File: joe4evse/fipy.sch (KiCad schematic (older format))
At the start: 2 parts

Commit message: joe/sch: Schematic should be done
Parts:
- added C4, C9: 100n, Capacitor_SMD:C_0603_1608Metric, symbol Device:C_Small
- added D3, D4: Green, LED_SMD:LED_0603_1608Metric, symbol Device:LED
- added R3, R4: 1k, Resistor_SMD:R_0603_1608Metric, symbol Device:R_Small
- added U4: MCP23S08-SO, Package_SO:SOIC-18W_7.5x11.6mm_P1.27mm, symbol ma4evse:MCP23S08-SO
- gave numbers to parts that had none: 2
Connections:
- net NFC_NRSTOUT is gone; now on net NFC_IRQ: U3.15 (P13)
- net +3V3: now also C4.2, C9.2, D3.2 (A), U4.18 (VCC)
- net +5V: now also D4.2 (A)
- net GND: now also C4.1, C9.1, R3.2, R4.2, U4.4 (A1), U4.5 (A0), U4.9 (GND)
- net MOD_EN: now also U4.12 (IO2); no longer U3.24 (P22)
- net NFC_IRQ: no longer U3.18 (P16)
- net FIPY_RX renamed RXD
- net FIPY_TX renamed TXD
- net FTDI_RX renamed LED_~CS
- net FTDI_TX renamed NFC_~CS
- net GPIO_P12: no longer names the net of U3.14 (ANT/P12)
- net GPIO_P2 renamed DEV_~RST
- net DEV_~RST: now also U4.6 (~RST)
- net GPIO_P21 renamed PP_IN
- net NFC_CLK renamed SCLK
- net SCLK: now also U4.1 (SCK)
- net NFC_MISO renamed MISO
- net MISO: now also U4.3 (SOUT)
- net NFC_MOSI renamed MOSI
- net MOSI: now also U4.2 (SIN)
- net NFC_NRST renamed IO_~CS
- net IO_~CS: now also U4.7 (~CS)
- net NFC_SS renamed TEMP
- net RELAY renamed PILOT_IN
- new net: D3.1 (K), R3.1
- new net: D4.1 (K), R4.1
- new net AC_TEST0: U4.14 (IO4)
- new net AC_TEST1: U4.15 (IO5)
- new net IO_IRQ: U3.18 (P16), U4.8 (INT)
- new net PILOT_OUT: U3.24 (P22)
- new net RCMB_AC_30mA: U4.17 (IO7)
- new net RCMB_DC_6mA: U4.16 (IO6)
- new net RELAY_AC: U4.11 (IO1)
- new net RELAY_JACK: U4.10 (IO0)
- new net TOUCH: U4.13 (IO3)
- no-connect marks 8 -> 9
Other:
- note added: "AC power verification signals"
- note added: "Charge port signals"
- note added: "Global SPI bus"
- note added: "Misc device control signals"
- note added: "Misc devices data signals"
- note added: "Power relays signals"
- note added: "Power status LEDs"
- note added: "Programming/ModBUS combined UART"
- note removed: "DHT11"
- note removed: "pin_out = \nP10\nP11\nP12\nP8\nP9"
- note removed: "uartm == UART0 = EV Controller\nSPI_PINS = RFID @1M == P10 P11 P12\nModbus = SmartMeter\n"
- moved on the sheet: J8, U3

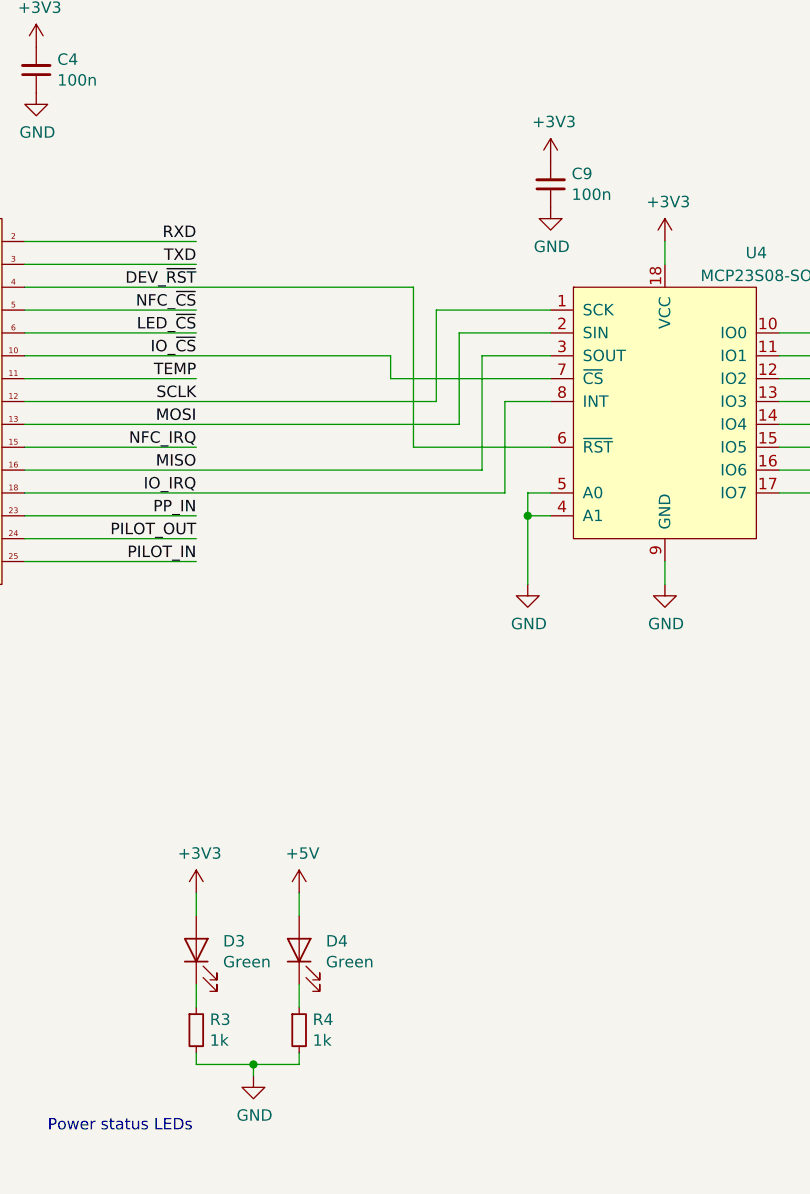
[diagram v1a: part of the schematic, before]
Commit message: joe/sch: Assign footprints to components
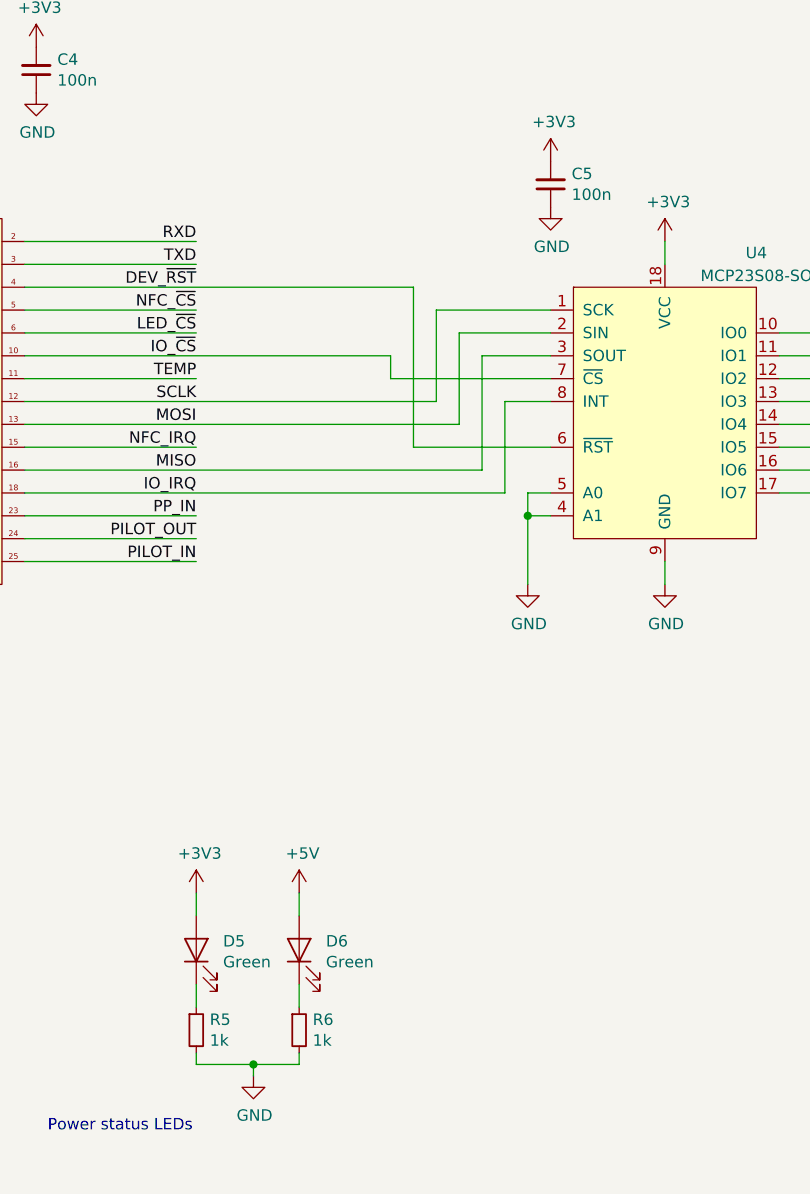
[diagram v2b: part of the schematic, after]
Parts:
- renumbered C9 to C5, D3 to D5, D4 to D6, R3 to R5, R4 to R6
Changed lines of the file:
@@
 	2800 2150 2900 2150
 $Comp
-L power:GND #PWR016
+L power:GND #PWR033
 U 1 1 5DD69575
 P 2900 2250
-F 0 "#PWR016" H 2900 2000 50  0001 C CNN
+F 0 "#PWR033" H 2900 2000 50  0001 C CNN
 F 1 "GND" H 2905 2077 50  0000 C CNN
 F 2 "" H 2900 2250 50  0001 C CNN
@@
 	4950 3550 4950 3650
 $Comp
-L power:GND #PWR019
+L power:GND #PWR036
 U 1 1 5DD69582
 P 4950 3650
-F 0 "#PWR019" H 4950 3400 50  0001 C CNN
+F 0 "#PWR036" H 4950 3400 50  0001 C CNN
 F 1 "GND" H 4955 3477 50  0000 C CNN
 F 2 "" H 4950 3650 50  0001 C CNN
@@
 	4850 1650 4850 1750
 $Comp
-L power:+3V3 #PWR014
+L power:+3V3 #PWR030
 U 1 1 5DD6958A
 P 5050 1650
-F 0 "#PWR014" H 5050 1500 50  0001 C CNN
+F 0 "#PWR030" H 5050 1500 50  0001 C CNN
 F 1 "+3V3" H 5065 1823 50  0000 C CNN
 F 2 "" H 5050 1650 50  0001 C CNN
@@
 $EndComp
 $Comp
-L power:+5V #PWR013
+L power:+5V #PWR029
 U 1 1 5DD69590
 P 4850 1650
-F 0 "#PWR013" H 4850 1500 50  0001 C CNN
+F 0 "#PWR029" H 4850 1500 50  0001 C CNN
 F 1 "+5V" H 4865 1823 50  0000 C CNN
 F 2 "" H 4850 1650 50  0001 C CNN
@@
 	5700 2450 7300 2450
 $Comp
-L power:GND #PWR017
+L power:GND #PWR034
 U 1 1 5E1CCCF4
 P 7900 3450
-F 0 "#PWR017" H 7900 3200 50  0001 C CNN
+F 0 "#PWR034" H 7900 3200 50  0001 C CNN
 F 1 "GND" H 7905 3277 50  0000 C CNN
 F 2 "" H 7900 3450 50  0001 C CNN
@@
 $EndComp
 $Comp
-L power:GND #PWR018
+L power:GND #PWR035
 U 1 1 5E1CD7DB
 P 8500 3450
-F 0 "#PWR018" H 8500 3200 50  0001 C CNN
+F 0 "#PWR035" H 8500 3200 50  0001 C CNN
 F 1 "GND" H 8505 3277 50  0000 C CNN
 F 2 "" H 8500 3450 50  0001 C CNN
@@
 $EndComp
 $Comp
-L power:+3V3 #PWR015
+L power:+3V3 #PWR032
 U 1 1 5E1CDD5F
 P 8500 1950
-F 0 "#PWR015" H 8500 1800 50  0001 C CNN
+F 0 "#PWR032" H 8500 1800 50  0001 C CNN
 F 1 "+3V3" H 8515 2123 50  0000 C CNN
 F 2 "" H 8500 1950 50  0001 C CNN
@@
 P 6450 5050
 AR Path="/5E261C05" Ref="D?"  Part="1"
-AR Path="/5DD371FF/5E261C05" Ref="D3"  Part="1"
-F 0 "D3" V 6489 4933 50  0000 R CNN
+AR Path="/5DD371FF/5E261C05" Ref="D5"  Part="1"
+F 0 "D5" V 6489 4933 50  0000 R CNN
 F 1 "Green" V 6398 4933 50  0000 R CNN
 F 2 "LED_SMD:LED_0603_1608Metric" H 6450 5050 50  0001 C CNN
@@
 P 6900 5050
 AR Path="/5E261C0B" Ref="D?"  Part="1"
-AR Path="/5DD371FF/5E261C0B" Ref="D4"  Part="1"
-F 0 "D4" V 6939 4933 50  0000 R CNN
+AR Path="/5DD371FF/5E261C0B" Ref="D6"  Part="1"
+F 0 "D6" V 6939 4933 50  0000 R CNN
 F 1 "Green" V 6848 4933 50  0000 R CNN
 F 2 "LED_SMD:LED_0603_1608Metric" H 6900 5050 50  0001 C CNN
@@
 P 6450 4800
 AR Path="/5E261C11" Ref="#PWR?"  Part="1"
-AR Path="/5DD371FF/5E261C11" Ref="#PWR020"  Part="1"
-F 0 "#PWR020" H 6450 4650 50  0001 C CNN
+AR Path="/5DD371FF/5E261C11" Ref="#PWR037"  Part="1"
+F 0 "#PWR037" H 6450 4650 50  0001 C CNN
 F 1 "+3V3" H 6465 4973 50  0000 C CNN
 F 2 "" H 6450 4800 50  0001 C CNN
@@
 P 6900 4800
 AR Path="/5E261C17" Ref="#PWR?"  Part="1"
-AR Path="/5DD371FF/5E261C17" Ref="#PWR021"  Part="1"
-F 0 "#PWR021" H 6900 4650 50  0001 C CNN
+AR Path="/5DD371FF/5E261C17" Ref="#PWR038"  Part="1"
+F 0 "#PWR038" H 6900 4650 50  0001 C CNN
 F 1 "+5V" H 6915 4973 50  0000 C CNN
 F 2 "" H 6900 4800 50  0001 C CNN
@@
 P 6450 5400
 AR Path="/5E261C1D" Ref="R?"  Part="1"
-AR Path="/5DD371FF/5E261C1D" Ref="R3"  Part="1"
-F 0 "R3" H 6509 5446 50  0000 L CNN
+AR Path="/5DD371FF/5E261C1D" Ref="R5"  Part="1"
+F 0 "R5" H 6509 5446 50  0000 L CNN
 F 1 "1k" H 6509 5355 50  0000 L CNN
 F 2 "Resistor_SMD:R_0603_1608Metric" H 6450 5400 50  0001 C CNN
@@
 P 6900 5400
 AR Path="/5E261C23" Ref="R?"  Part="1"
-AR Path="/5DD371FF/5E261C23" Ref="R4"  Part="1"
-F 0 "R4" H 6959 5446 50  0000 L CNN
+AR Path="/5DD371FF/5E261C23" Ref="R6"  Part="1"
+F 0 "R6" H 6959 5446 50  0000 L CNN
 F 1 "1k" H 6959 5355 50  0000 L CNN
 F 2 "Resistor_SMD:R_0603_1608Metric" H 6900 5400 50  0001 C CNN
@@
 P 6700 5600
 AR Path="/5E261C29" Ref="#PWR?"  Part="1"
-AR Path="/5DD371FF/5E261C29" Ref="#PWR022"  Part="1"
-F 0 "#PWR022" H 6700 5350 50  0001 C CNN
+AR Path="/5DD371FF/5E261C29" Ref="#PWR039"  Part="1"
+F 0 "#PWR039" H 6700 5350 50  0001 C CNN
 F 1 "GND" H 6705 5427 50  0000 C CNN
 F 2 "" H 6700 5600 50  0001 C CNN
@@
 P 5750 1100
 AR Path="/5E265A91" Ref="#PWR?"  Part="1"
-AR Path="/5DD371FF/5E265A91" Ref="#PWR011"  Part="1"
-F 0 "#PWR011" H 5750 950 50  0001 C CNN
+AR Path="/5DD371FF/5E265A91" Ref="#PWR026"  Part="1"
+F 0 "#PWR026" H 5750 950 50  0001 C CNN
 F 1 "+3V3" H 5765 1273 50  0000 C CNN
 F 2 "" H 5750 1100 50  0001 C CNN
@@
 P 5750 1300
 AR Path="/5E265A97" Ref="#PWR?"  Part="1"
-AR Path="/5DD371FF/5E265A97" Ref="#PWR012"  Part="1"
-F 0 "#PWR012" H 5750 1050 50  0001 C CNN
+AR Path="/5DD371FF/5E265A97" Ref="#PWR027"  Part="1"
+F 0 "#PWR027" H 5750 1050 50  0001 C CNN
 F 1 "GND" H 5755 1127 50  0000 C CNN
 F 2 "" H 5750 1300 50  0001 C CNN
@@
 P 8000 1700
 AR Path="/5E218F5F" Ref="C?"  Part="1"
-AR Path="/5DD371FF/5E218F5F" Ref="C9"  Part="1"
-F 0 "C9" H 7908 1654 50  0000 R CNN
+AR Path="/5DD371FF/5E218F5F" Ref="C5"  Part="1"
+F 0 "C5" H 7908 1654 50  0000 R CNN
 F 1 "100n" H 7908 1745 50  0000 R CNN
 F 2 "Capacitor_SMD:C_0603_1608Metric" H 8000 1700 50  0001 C CNN
@@
 P 8000 1600
 AR Path="/5E218F65" Ref="#PWR?"  Part="1"
-AR Path="/5DD371FF/5E218F65" Ref="#PWR0124"  Part="1"
-F 0 "#PWR0124" H 8000 1450 50  0001 C CNN
+AR Path="/5DD371FF/5E218F65" Ref="#PWR028"  Part="1"
+F 0 "#PWR028" H 8000 1450 50  0001 C CNN
 F 1 "+3V3" H 8015 1773 50  0000 C CNN
 F 2 "" H 8000 1600 50  0001 C CNN
@@
 P 8000 1800
 AR Path="/5E218F6B" Ref="#PWR?"  Part="1"
-AR Path="/5DD371FF/5E218F6B" Ref="#PWR0125"  Part="1"
-F 0 "#PWR0125" H 8000 1550 50  0001 C CNN
+AR Path="/5DD371FF/5E218F6B" Ref="#PWR031"  Part="1"
+F 0 "#PWR031" H 8000 1550 50  0001 C CNN
 F 1 "GND" H 8005 1627 50  0000 C CNN
 F 2 "" H 8000 1800 50  0001 C CNN

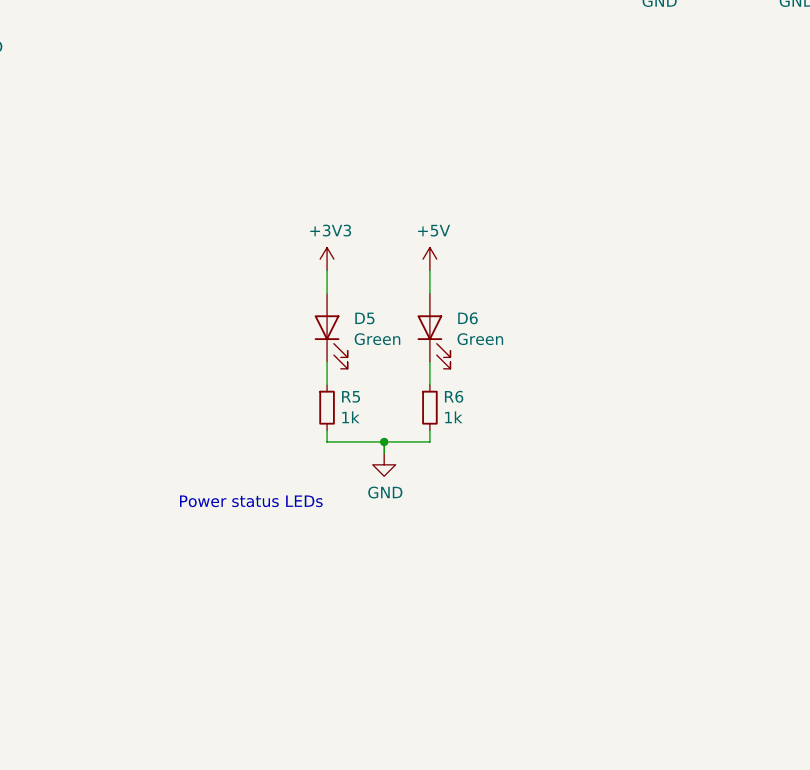
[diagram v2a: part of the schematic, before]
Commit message: joe/sch: Remove relays and only keep control circuitry
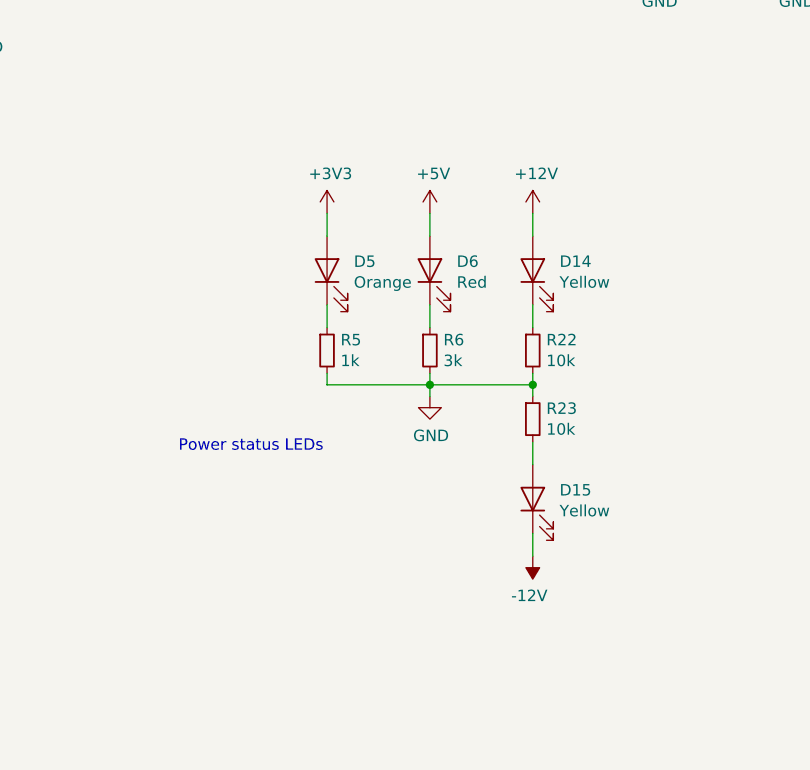
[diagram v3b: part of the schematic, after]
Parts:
- added D14, D15: Yellow, LED_SMD:LED_0603_1608Metric, symbol Device:LED
- added R22, R23: 10k, Resistor_SMD:R_0603_1608Metric, symbol Device:R_Small
- D5: value Green -> Orange
- D6: value Green -> Red
- R6: value 1k -> 3k
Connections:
- net GND: now also R22.2, R23.1
- new net: D14.1 (K), R22.1
- new net: D15.2 (A), R23.2
- new net +12V: D14.2 (A)
- new net -12V: D15.1 (K)
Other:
- moved on the sheet: D5, D6, R5, R6
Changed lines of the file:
@@
 $Descr A4 11693 8268
 encoding utf-8
-Sheet 2 6
+Sheet 2 3
 Title "Joe 4 EVSE"
 Date "2019-12-10"
@@
 L Device:LED D?
 U 1 1 5E261C05
-P 6450 5050
+P 6450 4800
 AR Path="/5E261C05" Ref="D?"  Part="1"
 AR Path="/5DD371FF/5E261C05" Ref="D5"  Part="1"
-F 0 "D5" V 6489 4933 50  0000 R CNN
-F 1 "Green" V 6398 4933 50  0000 R CNN
-F 2 "LED_SMD:LED_0603_1608Metric" H 6450 5050 50  0001 C CNN
-F 3 "~" H 6450 5050 50  0001 C CNN
-	1    6450 5050
+F 0 "D5" V 6489 4683 50  0000 R CNN
+F 1 "Orange" V 6398 4683 50  0000 R CNN
+F 2 "LED_SMD:LED_0603_1608Metric" H 6450 4800 50  0001 C CNN
+F 3 "~" H 6450 4800 50  0001 C CNN
+	1    6450 4800
 	0    -1   -1   0
 $EndComp
@@
 L Device:LED D?
 U 1 1 5E261C0B
-P 6900 5050
+P 6900 4800
 AR Path="/5E261C0B" Ref="D?"  Part="1"
 AR Path="/5DD371FF/5E261C0B" Ref="D6"  Part="1"
-F 0 "D6" V 6939 4933 50  0000 R CNN
-F 1 "Green" V 6848 4933 50  0000 R CNN
-F 2 "LED_SMD:LED_0603_1608Metric" H 6900 5050 50  0001 C CNN
-F 3 "~" H 6900 5050 50  0001 C CNN
-	1    6900 5050
+F 0 "D6" V 6939 4683 50  0000 R CNN
+F 1 "Red" V 6848 4683 50  0000 R CNN
+F 2 "LED_SMD:LED_0603_1608Metric" H 6900 4800 50  0001 C CNN
+F 3 "~" H 6900 4800 50  0001 C CNN
+	1    6900 4800
 	0    -1   -1   0
 $EndComp
@@
 L power:+3V3 #PWR?
 U 1 1 5E261C11
-P 6450 4800
+P 6450 4550
 AR Path="/5E261C11" Ref="#PWR?"  Part="1"
 AR Path="/5DD371FF/5E261C11" Ref="#PWR037"  Part="1"
-F 0 "#PWR037" H 6450 4650 50  0001 C CNN
-F 1 "+3V3" H 6465 4973 50  0000 C CNN
-F 2 "" H 6450 4800 50  0001 C CNN
-F 3 "" H 6450 4800 50  0001 C CNN
-	1    6450 4800
+F 0 "#PWR037" H 6450 4400 50  0001 C CNN
+F 1 "+3V3" H 6465 4723 50  0000 C CNN
+F 2 "" H 6450 4550 50  0001 C CNN
+F 3 "" H 6450 4550 50  0001 C CNN
+	1    6450 4550
 	1    0    0    -1
 $EndComp
@@
 L power:+5V #PWR?
 U 1 1 5E261C17
-P 6900 4800
+P 6900 4550
 AR Path="/5E261C17" Ref="#PWR?"  Part="1"
 AR Path="/5DD371FF/5E261C17" Ref="#PWR038"  Part="1"
-F 0 "#PWR038" H 6900 4650 50  0001 C CNN
-F 1 "+5V" H 6915 4973 50  0000 C CNN
-F 2 "" H 6900 4800 50  0001 C CNN
-F 3 "" H 6900 4800 50  0001 C CNN
-	1    6900 4800
+F 0 "#PWR038" H 6900 4400 50  0001 C CNN
+F 1 "+5V" H 6915 4723 50  0000 C CNN
+F 2 "" H 6900 4550 50  0001 C CNN
+F 3 "" H 6900 4550 50  0001 C CNN
+	1    6900 4550
 	1    0    0    -1
 $EndComp
@@
 L Device:R_Small R?
 U 1 1 5E261C1D
-P 6450 5400
+P 6450 5150
 AR Path="/5E261C1D" Ref="R?"  Part="1"
 AR Path="/5DD371FF/5E261C1D" Ref="R5"  Part="1"
-F 0 "R5" H 6509 5446 50  0000 L CNN
-F 1 "1k" H 6509 5355 50  0000 L CNN
-F 2 "Resistor_SMD:R_0603_1608Metric" H 6450 5400 50  0001 C CNN
-F 3 "~" H 6450 5400 50  0001 C CNN
-	1    6450 5400
+F 0 "R5" H 6509 5196 50  0000 L CNN
+F 1 "1k" H 6509 5105 50  0000 L CNN
+F 2 "Resistor_SMD:R_0603_1608Metric" H 6450 5150 50  0001 C CNN
+F 3 "~" H 6450 5150 50  0001 C CNN
+	1    6450 5150
 	1    0    0    -1
 $EndComp
@@
 L Device:R_Small R?
 U 1 1 5E261C23
-P 6900 5400
+P 6900 5150
 AR Path="/5E261C23" Ref="R?"  Part="1"
 AR Path="/5DD371FF/5E261C23" Ref="R6"  Part="1"
-F 0 "R6" H 6959 5446 50  0000 L CNN
-F 1 "1k" H 6959 5355 50  0000 L CNN
-F 2 "Resistor_SMD:R_0603_1608Metric" H 6900 5400 50  0001 C CNN
-F 3 "~" H 6900 5400 50  0001 C CNN
-	1    6900 5400
+F 0 "R6" H 6959 5196 50  0000 L CNN
+F 1 "3k" H 6959 5105 50  0000 L CNN
+F 2 "Resistor_SMD:R_0603_1608Metric" H 6900 5150 50  0001 C CNN
+F 3 "~" H 6900 5150 50  0001 C CNN
+	1    6900 5150
 	1    0    0    -1
 $EndComp
@@
 L power:GND #PWR?
 U 1 1 5E261C29
-P 6700 5600
+P 6900 5350
 AR Path="/5E261C29" Ref="#PWR?"  Part="1"
 AR Path="/5DD371FF/5E261C29" Ref="#PWR039"  Part="1"
-F 0 "#PWR039" H 6700 5350 50  0001 C CNN
-F 1 "GND" H 6705 5427 50  0000 C CNN
-F 2 "" H 6700 5600 50  0001 C CNN
-F 3 "" H 6700 5600 50  0001 C CNN
-	1    6700 5600
-	1    0    0    -1
-$EndComp
-Wire Wire Line
-	6450 4800 6450 4900
-Wire Wire Line
-	6450 5200 6450 5300
-Wire Wire Line
-	6450 5500 6450 5550
-Wire Wire Line
-	6450 5550 6700 5550
-Wire Wire Line
-	6900 5550 6900 5500
-Wire Wire Line
-	6900 5300 6900 5200
-Wire Wire Line
-	6900 4900 6900 4800
-Wire Wire Line
-	6700 5600 6700 5550
-Connection ~ 6700 5550
-Wire Wire Line
-	6700 5550 6900 5550
-Text Notes 5800 5850 0    50   ~ 0
+F 0 "#PWR039" H 6900 5100 50  0001 C CNN
+F 1 "GND" H 6905 5177 50  0000 C CNN
+F 2 "" H 6900 5350 50  0001 C CNN
+F 3 "" H 6900 5350 50  0001 C CNN
+	1    6900 5350
+	1    0    0    -1
+$EndComp
+Wire Wire Line
+	6450 4550 6450 4650
+Wire Wire Line
+	6450 4950 6450 5050
+Wire Wire Line
+	6450 5250 6450 5300
+Wire Wire Line
+	6900 5300 6900 5250
+Wire Wire Line
+	6900 5050 6900 4950
+Wire Wire Line
+	6900 4650 6900 4550
+Wire Wire Line
+	6900 5350 6900 5300
+Text Notes 5800 5600 0    50   ~ 0
 Power status LEDs
 $Comp
@@
 	1    0    0    -1
 $EndComp
+$Comp
+L Device:LED D?
+U 1 1 5E421888
+P 7350 4800
+AR Path="/5E421888" Ref="D?"  Part="1"
+AR Path="/5DD371FF/5E421888" Ref="D14"  Part="1"
+F 0 "D14" V 7389 4683 50  0000 R CNN
+F 1 "Yellow" V 7298 4683 50  0000 R CNN
+F 2 "LED_SMD:LED_0603_1608Metric" H 7350 4800 50  0001 C CNN
+F 3 "~" H 7350 4800 50  0001 C CNN
+	1    7350 4800
+	0    -1   -1   0
+$EndComp
+$Comp
+L Device:R_Small R?
+U 1 1 5E421C7D
+P 7350 5150
+AR Path="/5E421C7D" Ref="R?"  Part="1"
+AR Path="/5DD371FF/5E421C7D" Ref="R22"  Part="1"
+F 0 "R22" H 7409 5196 50  0000 L CNN
+F 1 "10k" H 7409 5105 50  0000 L CNN
+F 2 "Resistor_SMD:R_0603_1608Metric" H 7350 5150 50  0001 C CNN
+F 3 "~" H 7350 5150 50  0001 C CNN
+	1    7350 5150
+	1    0    0    -1
+$EndComp
+Connection ~ 6900 5300
+Wire Wire Line
+	6450 5300 6900 5300
+Wire Wire Line
+	6900 5300 7350 5300
+Wire Wire Line
+	7350 5300 7350 5250
+Wire Wire Line
+	7350 5050 7350 4950
+Wire Wire Line
+	7350 4650 7350 4550
+$Comp
+L power:+12V #PWR070
+U 1 1 5E42B1C9
+P 7350 4550
+F 0 "#PWR070" H 7350 4400 50  0001 C CNN
+F 1 "+12V" H 7365 4723 50  0000 C CNN
+F 2 "" H 7350 4550 50  0001 C CNN
+F 3 "" H 7350 4550 50  0001 C CNN
+	1    7350 4550
+	1    0    0    -1
+$EndComp
+$Comp
+L Device:R_Small R?
+U 1 1 5E42BD5D
+P 7350 5450
+AR Path="/5E42BD5D" Ref="R?"  Part="1"
+AR Path="/5DD371FF/5E42BD5D" Ref="R23"  Part="1"
+F 0 "R23" H 7409 5496 50  0000 L CNN
+F 1 "10k" H 7409 5405 50  0000 L CNN
+F 2 "Resistor_SMD:R_0603_1608Metric" H 7350 5450 50  0001 C CNN
+F 3 "~" H 7350 5450 50  0001 C CNN
+	1    7350 5450
+	1    0    0    -1
+$EndComp
+$Comp
+L Device:LED D?
+U 1 1 5E42C07B
+P 7350 5800
+AR Path="/5E42C07B" Ref="D?"  Part="1"
+AR Path="/5DD371FF/5E42C07B" Ref="D15"  Part="1"
+F 0 "D15" V 7389 5683 50  0000 R CNN
+F 1 "Yellow" V 7298 5683 50  0000 R CNN
+F 2 "LED_SMD:LED_0603_1608Metric" H 7350 5800 50  0001 C CNN
+F 3 "~" H 7350 5800 50  0001 C CNN
+	1    7350 5800
+	0    -1   -1   0
+$EndComp
+$Comp
+L power:-12V #PWR071
+U 1 1 5E42C65B
+P 7350 6050
+F 0 "#PWR071" H 7350 6150 50  0001 C CNN
+F 1 "-12V" H 7365 6223 50  0000 C CNN
+F 2 "" H 7350 6050 50  0001 C CNN
+F 3 "" H 7350 6050 50  0001 C CNN
+	1    7350 6050
+	-1   0    0    1
+$EndComp
+Wire Wire Line
+	7350 5300 7350 5350
+Connection ~ 7350 5300
+Wire Wire Line
+	7350 5550 7350 5650
+Wire Wire Line
+	7350 5950 7350 6050
 $EndSCHEMATC
